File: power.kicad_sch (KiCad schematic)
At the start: 34 parts, among them J6 Battery In, J7 Conn_01x02_Socket, U12 LM1084-3.3, U13 TLV4387, U15 TVS0500DRV, U6 TPS22929D, U7 REF3040, U8 REF3025, U9 ESDA5V3SC5

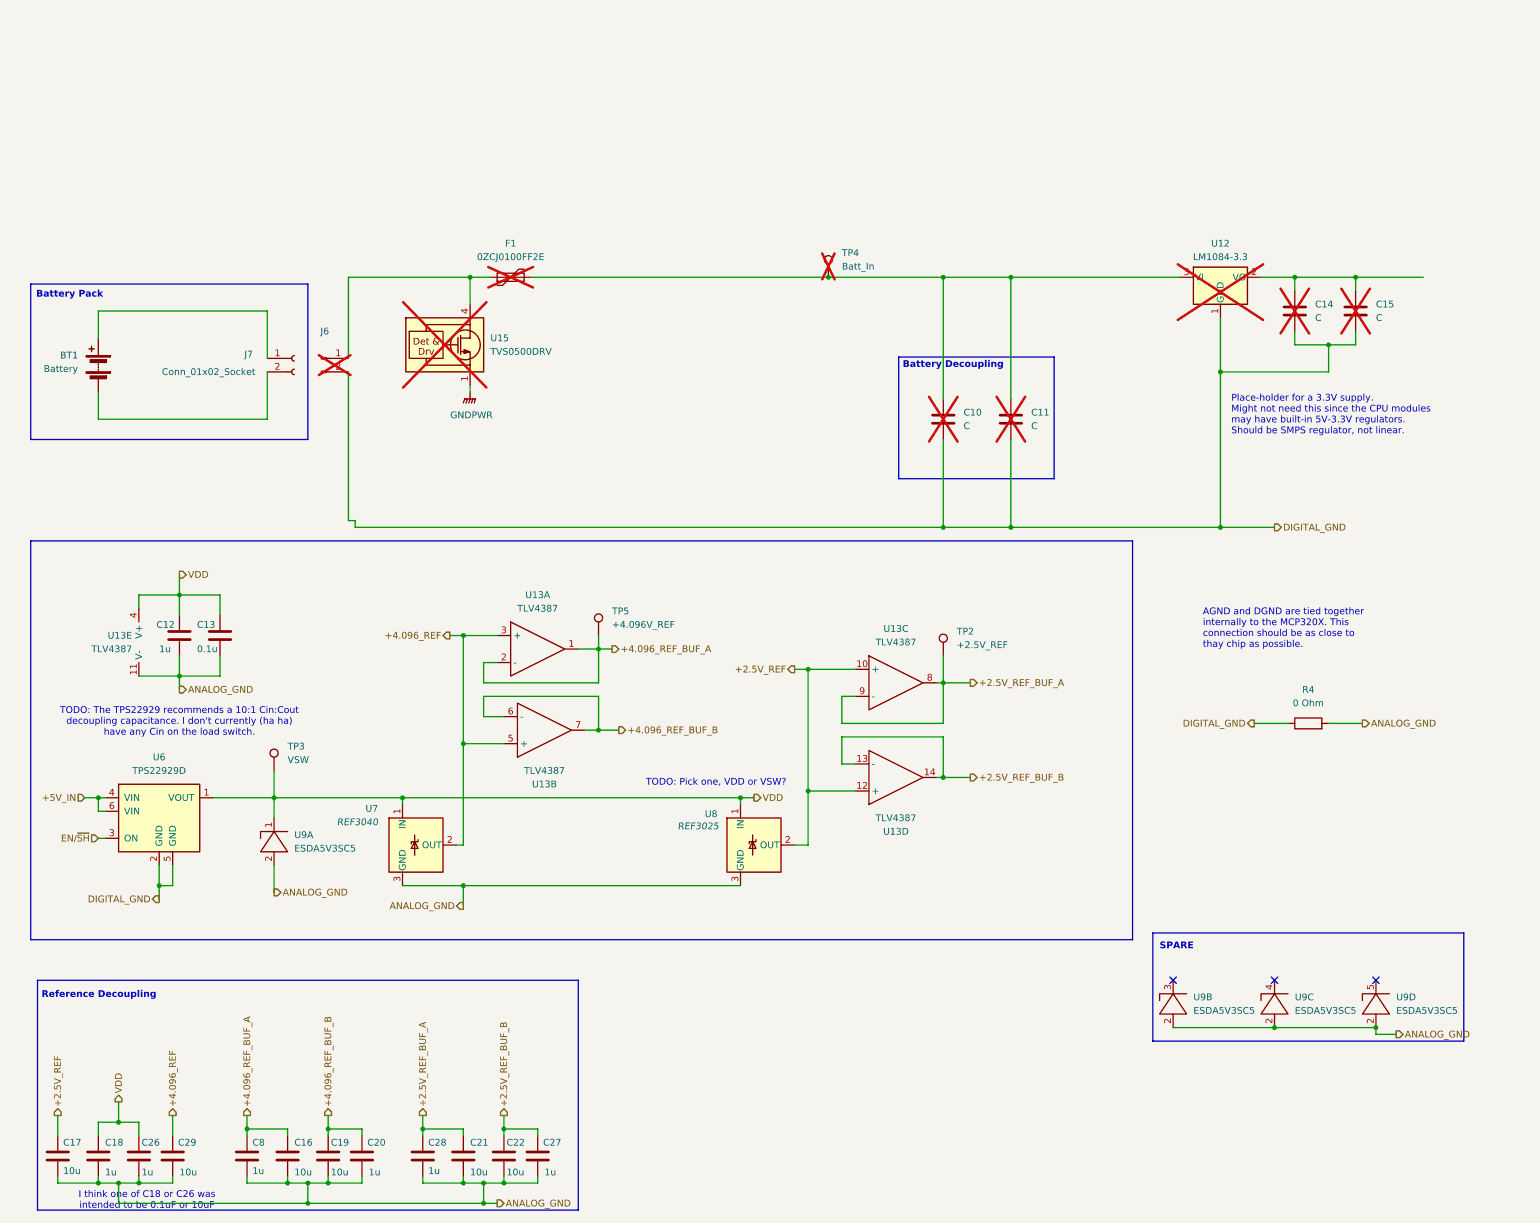
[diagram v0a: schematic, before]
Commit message: Prototype v0.3.1 WIP Just a maintenance checkin. Many changes - Removed the Base Sensor schematic and put all sensors into SensorPrototype - Added a constant current LED driver for camera illumination - Added a 12V buck converter to the input in support of external power - Added a low-side current sense to the input - Added an LDO regulator to cleanup Buck output and to provide battery regulation - Added support for an internal battery + switchover / charge circuit. - Swapped headers for proper board connectors - Added an RS485 transceiver for external + modem communication - Added an additional temperature circuit in support of NTC probes - Incorporated the AS Dissolved Oxygen sensor into the main board - Added DC return path resistors to non-inverting amps - Fixed mixed power domain bug - Moved AS isolated carrier board to 3.3V rail and routed the shutdown pin to en/sh - Moved the DHT20 to the 3.3V rail - In the process of re-routing ADC channels.
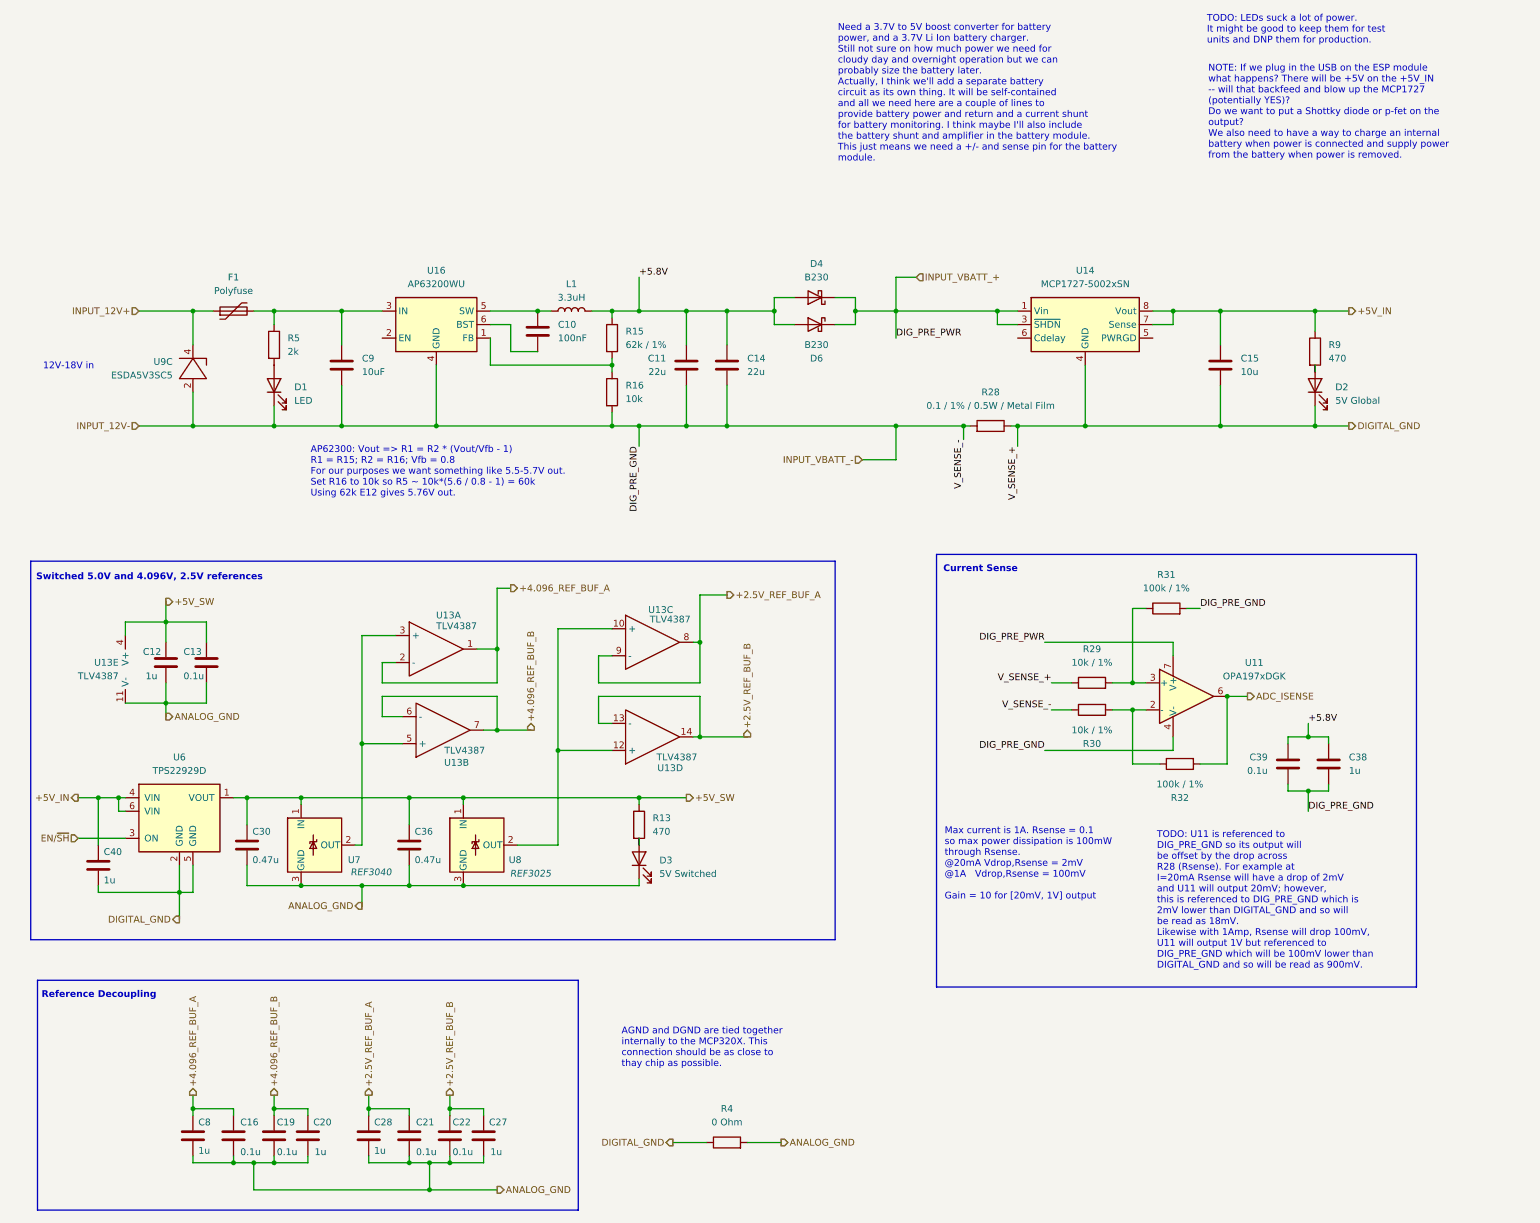
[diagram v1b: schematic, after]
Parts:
- removed BT1: Battery, symbol Device:Battery
- removed C17, C29: 10u, Capacitor_SMD:C_1210_3225Metric_Pad1.33x2.70mm_HandSolder, symbol Device:C
- removed C18, C26: 1u, Capacitor_SMD:C_1210_3225Metric_Pad1.33x2.70mm_HandSolder, symbol Device:C
- removed J6: Battery In, Connector_PinHeader_2.54mm:PinHeader_1x02_P2.54mm_Vertical_SMD_Pin1Left, symbol Connector:Conn_01x02_Pin
- removed J7: Conn_01x02_Socket, symbol Connector:Conn_01x02_Socket
- removed TP2: +2.5V_REF, TestPoint:TestPoint_Pad_D3.0mm, symbol Connector:TestPoint
- removed TP3: VSW, TestPoint:TestPoint_Pad_D3.0mm, symbol Connector:TestPoint
- removed TP4: Batt_In, TestPoint:TestPoint_Pad_D3.0mm, symbol Connector:TestPoint
- removed TP5: +4.096V_REF, TestPoint:TestPoint_Pad_D3.0mm, symbol Connector:TestPoint
- removed U12: LM1084-3.3, Connector_PinHeader_2.54mm:PinHeader_2x10_P2.54mm_Vertical_SMD, symbol Regulator_Linear:LM1084-3.3
- removed U15: TVS0500DRV, Package_SON:WSON-6-1EP_2x2mm_P0.65mm_EP1x1.6mm, symbol Power_Protection:TVS0500DRV
- removed unit 4 of U9
- removed unit 2 of U9
- removed unit 1 of U9
- added C30, C36: 0.47u, Capacitor_SMD:C_0805_2012Metric_Pad1.18x1.45mm_HandSolder, symbol Device:C
- added C38, C40: 1u, Capacitor_SMD:C_0805_2012Metric_Pad1.18x1.45mm_HandSolder, symbol Device:C
- added C39: 0.1u, Capacitor_SMD:C_0805_2012Metric_Pad1.18x1.45mm_HandSolder, symbol Device:C
- added C9: 10uF, Capacitor_SMD:C_0805_2012Metric_Pad1.18x1.45mm_HandSolder, symbol Device:C
- added D1: LED, LED_SMD:LED_0805_2012Metric_Pad1.15x1.40mm_HandSolder, symbol Device:LED
- added D2: 5V Global, LED_SMD:LED_0805_2012Metric_Pad1.15x1.40mm_HandSolder, symbol Device:LED
- added D3: 5V Switched, LED_SMD:LED_0805_2012Metric_Pad1.15x1.40mm_HandSolder, symbol Device:LED
- added D4, D6: B230, Diode_SMD:D_SMB, symbol Diode:B230
- added L1: 3.3uH, Inductor_SMD:L_1210_3225Metric_Pad1.42x2.65mm_HandSolder, symbol Device:L
- added R13, R9: 470, Resistor_SMD:R_0805_2012Metric_Pad1.20x1.40mm_HandSolder, symbol Device:R
- added R15: 62k / 1%, Resistor_SMD:R_0805_2012Metric_Pad1.20x1.40mm_HandSolder, symbol Device:R
- added R16: 10k, Resistor_SMD:R_0805_2012Metric_Pad1.20x1.40mm_HandSolder, symbol Device:R
- added R28: 0.1 / 1% / 0.5W / Metal Film, Resistor_SMD:R_1206_3216Metric, symbol Device:R
- added R29, R30: 10k / 1%, Resistor_SMD:R_0805_2012Metric_Pad1.20x1.40mm_HandSolder, symbol Device:R
- added R31, R32: 100k / 1%, Resistor_SMD:R_0805_2012Metric_Pad1.20x1.40mm_HandSolder, symbol Device:R
- added R5: 2k, Resistor_SMD:R_0805_2012Metric_Pad1.20x1.40mm_HandSolder, symbol Device:R
- added U11: OPA197xDGK, Package_SO:VSSOP-8_3x3mm_P0.65mm, symbol Amplifier_Operational:OPA197xDGK
- added U14: MCP1727-5002xSN, Package_SO:SOIC-8_3.9x4.9mm_P1.27mm, symbol Regulator_Linear:MCP1727-5002xSN
- added U16: AP63200WU, Package_TO_SOT_SMD:TSOT-23-6, symbol Regulator_Switching:AP63200WU
- C10: value C -> 100nF; footprint Capacitor_SMD:C_1210_3225Metric_Pad1.33x2.70mm_HandSolder -> Capacitor_SMD:C_0805_2012Metric_Pad1.18x1.45mm_HandSolder; now fitted; now in the parts list
- C11, C14: value C -> 22u; footprint Capacitor_SMD:C_1210_3225Metric_Pad1.33x2.70mm_HandSolder -> Capacitor_SMD:C_0805_2012Metric_Pad1.18x1.45mm_HandSolder; now fitted; now in the parts list
- C12, C13, C20, C27, C28, C8: footprint Capacitor_SMD:C_1210_3225Metric_Pad1.33x2.70mm_HandSolder -> Capacitor_SMD:C_0805_2012Metric_Pad1.18x1.45mm_HandSolder
- C15: value C -> 10u; footprint Capacitor_SMD:C_1210_3225Metric_Pad1.33x2.70mm_HandSolder -> Capacitor_SMD:C_0805_2012Metric_Pad1.18x1.45mm_HandSolder; now fitted; now in the parts list
- C16, C19, C21, C22: value 10u -> 0.1u; footprint Capacitor_SMD:C_1210_3225Metric_Pad1.33x2.70mm_HandSolder -> Capacitor_SMD:C_0805_2012Metric_Pad1.18x1.45mm_HandSolder
- F1: value 0ZCJ0100FF2E -> Polyfuse; footprint Fuse:Fuse_1206_3216Metric_Pad1.42x1.75mm_HandSolder -> (none); now fitted; now in the parts list
- R4: footprint Resistor_SMD:R_1210_3225Metric_Pad1.30x2.65mm_HandSolder -> Resistor_SMD:R_1206_3216Metric_Pad1.30x1.75mm_HandSolder
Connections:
- net +5V_IN: now also C15.1, C40.1, R9.1, U14.7 (Sense), U14.8 (Vout)
- net ANALOG_GND: now also C30.2, C36.2, D3.1 (K); no longer U9.2
- net DIGITAL_GND: now also C40.2, D2.1 (K), R28.1, R29.1, U14.4 (GND); no longer C10.2, C11.2, C14.2
- net INPUT_12V+: now reaches U9.4
- net INPUT_12V+: now also F1.1
- net +5.8V: now reaches C14.1
- net +5.8V: now also C11.1, C38.1, C39.1, D4.2 (A), D6.2 (A), L1.2, R15.2; no longer C15.1
- net +2.5V_REF: no longer names the net of U13.10 (+), U13.12 (+), U8.2 (OUT)
- net +4.096_REF: no longer names the net of U13.3 (+), U13.5 (+), U7.2 (OUT)
- net VDD renamed +5V_SW
- net +5V_SW: now also C30.1, C36.1, R13.1
- new net: D3.2 (A), R13.2
- new net: D2.2 (A), R9.2
- new net: R15.1, R16.1, U16.1 (FB)
- new net: C9.1, F1.2, R5.1, U16.3 (IN)
- new net: D1.2 (A), R5.2
- new net: C10.2, L1.1, U16.5 (SW)
- new net: C10.1, U16.6 (BST)
- new net: R30.2, R32.1, U11.2 (-)
- new net: R29.2, R31.1, U11.3 (+)
- new net ADC_ISENSE: R32.2, U11.6
- new net INPUT_12V-: C11.2, C14.2, C38.2, C39.2, C9.2, D1.1 (K), R16.2, R28.2, R30.1, R31.2, U11.4 (V-), U16.4 (GND), U9.2
- new net INPUT_VBATT_+: D4.1 (K), D6.1 (K), U11.7 (V+), U14.1 (Vin), U14.2 (Vin), U14.3 (~{SHDN})
- no-connect marks 3 -> 0
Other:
- note added: "12V-18V in"
- note added: "AP62300: Vout => R1 = R2 * (Vout/Vfb - 1) R1 = R15; R2 = R16; Vfb = 0.8 For our purposes we want something like 5.5-5.7V out. Set R16 to 10k so R5 ~ 10k*(5.6 / 0.8 - 1) = 60k Using 62k E12 gives 5.76V out."
- note added: "Current Sense"
- note added: "Max current is 1A. Rsense = 0.1 so max power dissipation is 100mW through Rsense. @20mA Vdrop,Rsense = 2mV @1A Vdrop,Rsense = 100mV Gain = 10 for [20mV, 1V] output"
- note added: "NOTE: If we plug in the USB on the ESP module what happens? There will be +5V on the +5V_IN -- will that backfeed and blow up the MCP1727 (potentially YES)? Do we want to put a Shottky diode or p-fet on the output? We also need to have a way to charge an internal battery when power is connected and supply power from the battery when power is removed."
- note added: "Need a 3.7V to 5V boost converter for battery power, and a 3.7V Li Ion battery charger. Still not sure on how much power we need for cloudy day and overnight operation but we can probably size the battery later. Actually, I think we'll add a separate battery circuit as its own thing. It will be self-contained and all we need here are a couple of lines to provide battery power and return and a cur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"
- note added: "Switched 5.0V and 4.096V, 2.5V references"
- note added: "TODO: LEDs suck a lot of power. It might be good to keep them for test units and DNP them for production."
- note added: "TODO: U11 is referenced to DIG_PRE_GND so its output will be offset by the drop across R28 (Rsense). For example at I=20mA Rsense will have a drop of 2mV and U11 will output 20mV; however, this is referenced to DIG_PRE_GND which is 2mV lower than DIGITAL_GND and so will be read as 18mV. Likewise with 1Amp, Rsense will drop 100mV, U11 will output 1V but referenced to DIG_PRE_GND which will be 100m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"
- note removed: "Battery Decoupling"
- note removed: "Battery Pack"
- note removed: "I think one of C18 or C26 was intended to be 0.1uF or 10uF"
- note removed: "Place-holder for a 3.3V supply. Might not need this since the CPU modules may have built-in 5V-3.3V regulators. Should be SMPS regulator, not linear."
- note removed: "SPARE"
- note removed: "TODO: Pick one, VDD or VSW?"
- note removed: "TODO: The TPS22929 recommends a 10:1 Cin:Cout decoupling capacitance. I don't currently (ha ha) have any Cin on the load switch."
- moved on the sheet: C12, C13, C16, C19, C20, C21, C22, C27, C28, C8, R4, U13A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

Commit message: Board V0.0.3 Everything is routed and connected ERC and DRC run without serious error. (There are DRC violations due to a VSSP-83x3mm package but I'm not sure why)
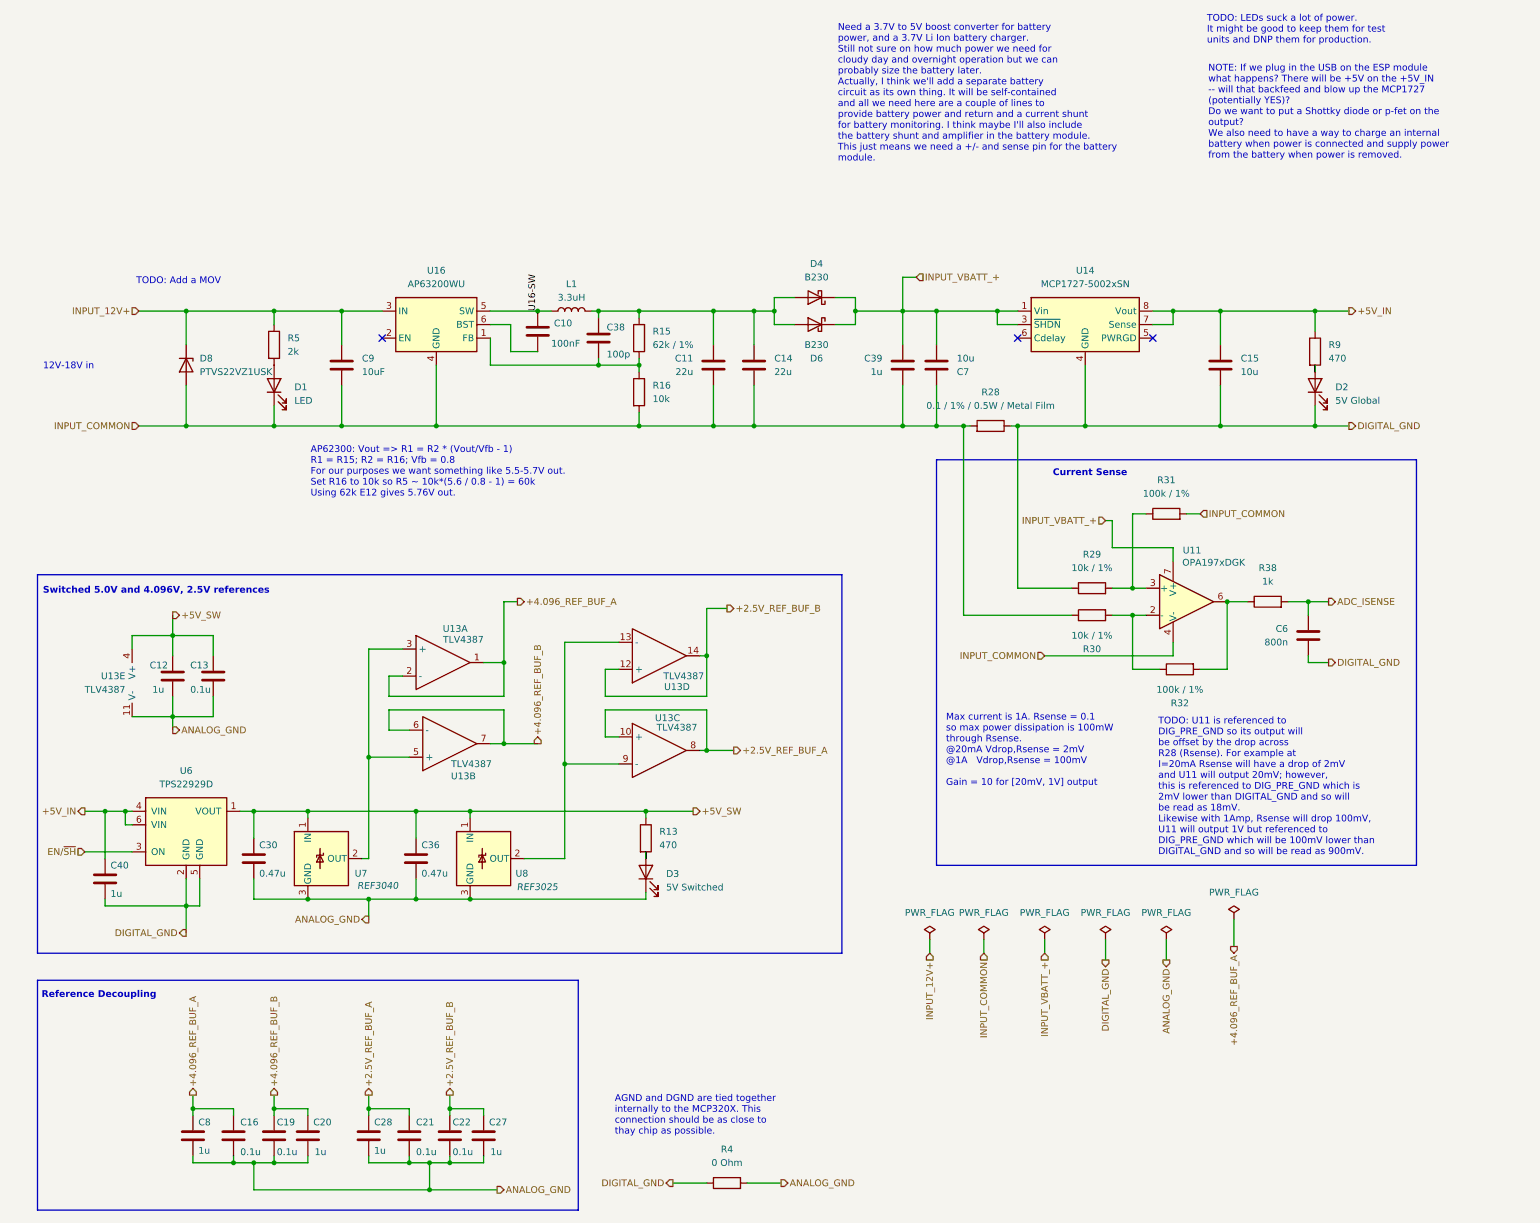
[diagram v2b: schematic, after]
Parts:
- removed F1: Polyfuse, symbol Device:Polyfuse
- removed U9: ESDA5V3SC5, Package_TO_SOT_SMD:SOT-23-5, symbol AndrewAdditions:sda5v3sc6_split
- added C6: 800n, Capacitor_SMD:C_0805_2012Metric_Pad1.18x1.45mm_HandSolder, symbol Device:C
- added C7: 10u, Capacitor_SMD:C_0805_2012Metric_Pad1.18x1.45mm_HandSolder, symbol Device:C
- added D8: PTVS22VZ1USK, Diode_SMD:Nexperia_DSN1608-2_1.6x0.8mm, symbol Diode:PTVS22VZ1USK
- added R38: 1k, Resistor_SMD:R_0805_2012Metric_Pad1.20x1.40mm_HandSolder, symbol Device:R
- C38: value 1u -> 100p
- C39: value 0.1u -> 1u
- R28: footprint Resistor_SMD:R_1206_3216Metric -> Resistor_SMD:R_1206_3216Metric_Pad1.30x1.75mm_HandSolder
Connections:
- net +2.5V_REF_BUF_A: now also U13.10 (+); no longer U13.9 (-)
- net +2.5V_REF_BUF_B: now also U13.12 (+); no longer U13.13 (-)
- net ADC_ISENSE: now also C6.1, R38.2; no longer R32.2, U11.6
- net DIGITAL_GND: now also C6.2
- net INPUT_12V+: now also C9.1, R5.1, U16.3 (IN), D8.1 (K)
- net INPUT_VBATT_+: now also C39.1, C7.2
- net at R15.1, R16.1, U16.1 (FB): now also C38.2
- net U16-SW: now reaches C10.2, L1.1, U16.5 (SW)
- net +5.8V: no longer names the net of C11.1, C14.1, C38.1, D4.2 (A), D6.2 (A), L1.2, R15.2
- net +5.8V: no longer C39.1
- net INPUT_12V- renamed INPUT_COMMON
- net INPUT_COMMON: now also C7.1, D8.2 (A); no longer C38.2
- new net: R32.2, R38.1, U11.6
- new net: U13.13 (-), U13.9 (-), U8.2 (OUT)
- no-connect marks 0 -> 3
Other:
- note added: "TODO: Add a MOV"
- moved on the sheet: C11, C12, C13, C14, C30, C36, C39, C40, D3, R13, R15, R16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
